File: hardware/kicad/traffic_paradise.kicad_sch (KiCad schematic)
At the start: 58 parts, among them J2 USB C, Q1 SS8050, Q2 SS8050, SW1 SW_Push, SW2 SW_Push, SW3 SW_Push, U1 ESP32-WROOM-32, U2 AMS1117-3.3, U3 USBLC6-2SC6, U4 CP2102N-A02-GQFN28

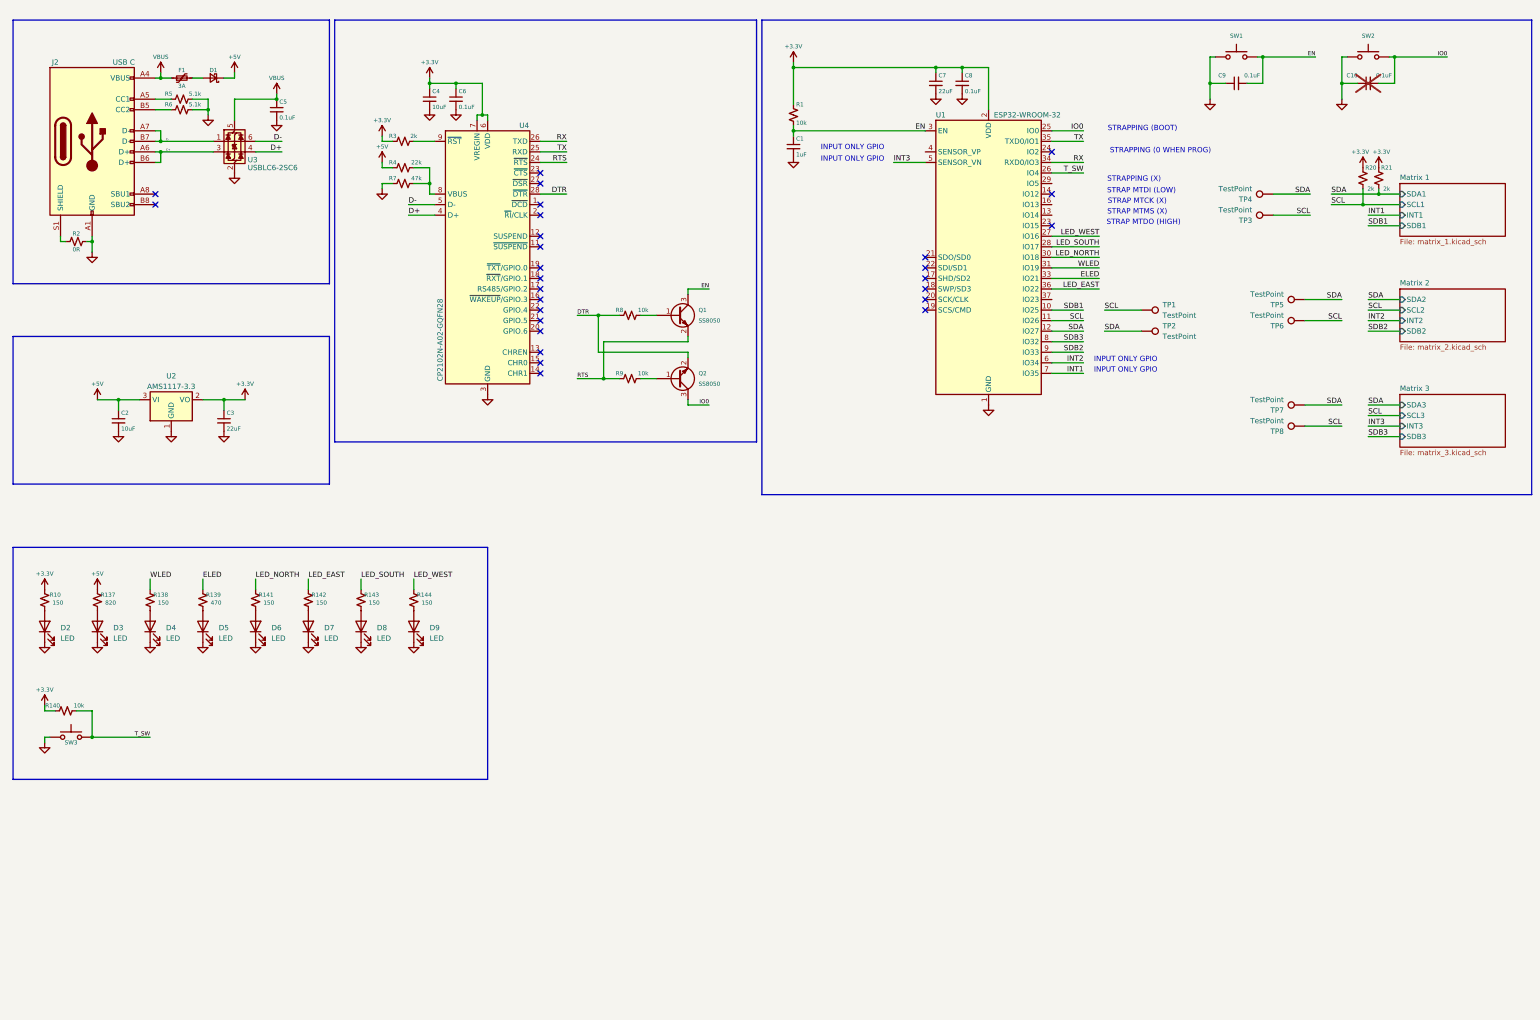
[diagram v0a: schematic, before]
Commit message: add jtag circuitry
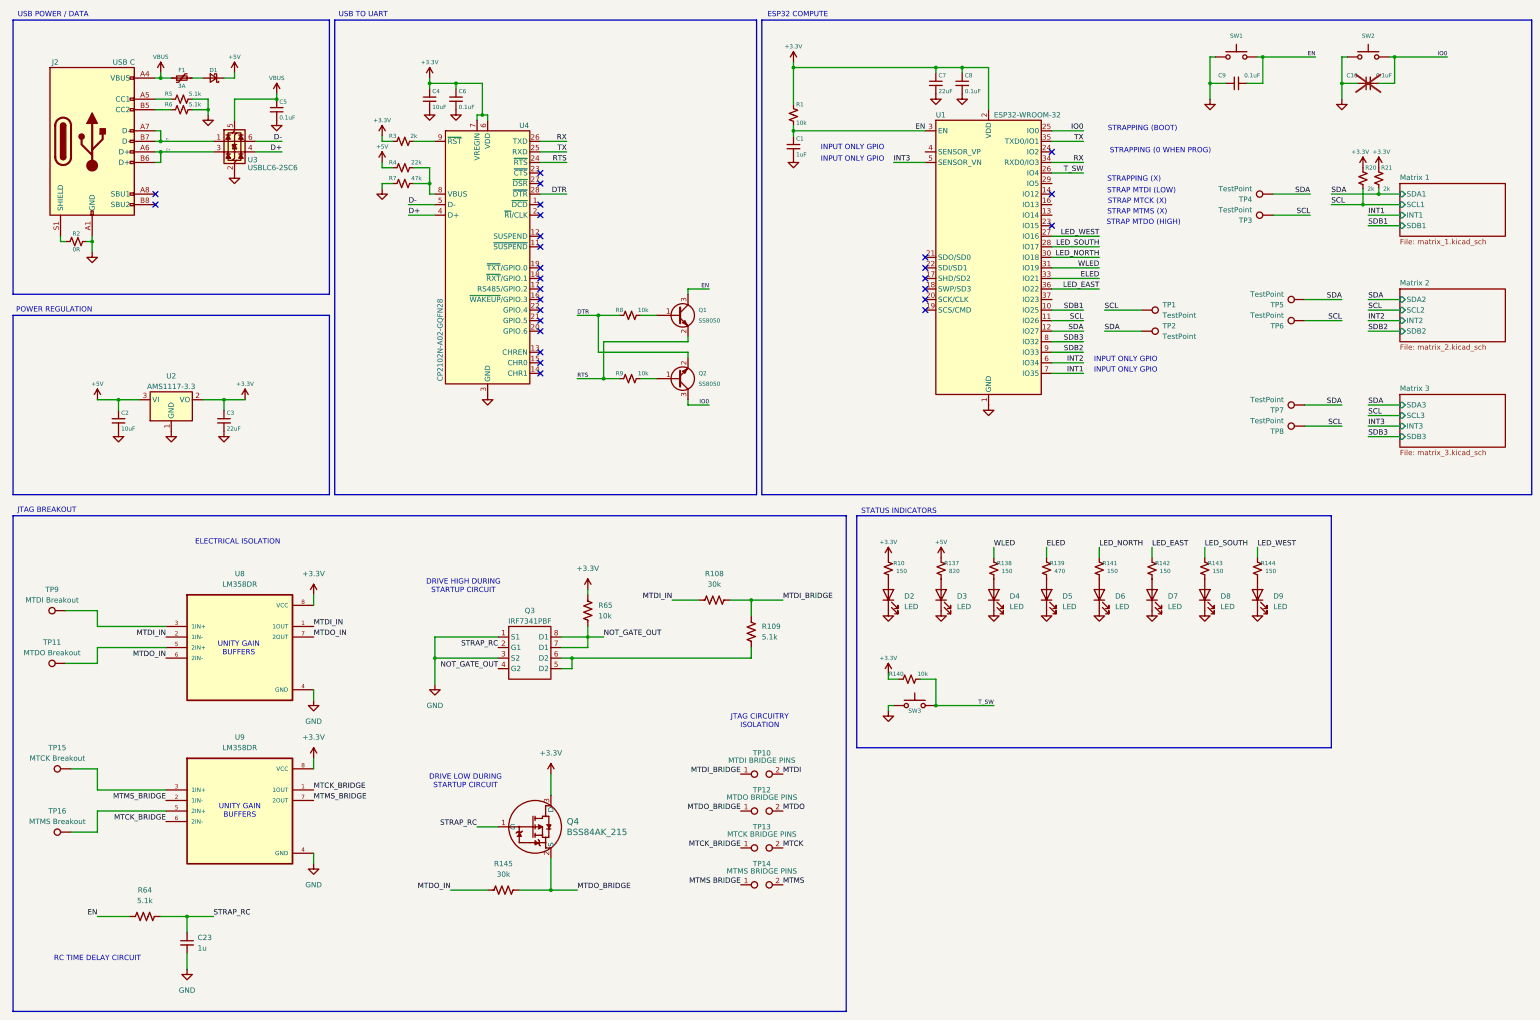
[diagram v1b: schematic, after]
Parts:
- added C23: 1u, Capacitor_SMD:C_0402_1005Metric, symbol Device:C_Small
- added Q3: IRF7341PBF, Package_SO:SOIC-8_3.9x4.9mm_P1.27mm, symbol IRF7341PBF:IRF7341PBF
- added Q4: BSS84AK_215, map_lbr:SOT23-BSS84AK_NEX, symbol BSS84AK215:BSS84AK_215
- added R108, R145: 30k, Resistor_SMD:R_0402_1005Metric, symbol Device:R_US
- added R109, R64: 5.1k, Resistor_SMD:R_0402_1005Metric, symbol Device:R_US
- added R65: 10k, Resistor_SMD:R_0603_1608Metric, symbol Device:R_US
- added TP10: MTDI BRIDGE PINS, TestPoint:TestPoint_Bridge_Pitch5.08mm_Drill1.3mm, symbol Connector:TestPoint_2Pole
- added TP11: MTDO Breakout, TestPoint:TestPoint_THTPad_D2.5mm_Drill1.2mm, symbol Connector:TestPoint
- added TP12: MTDO BRIDGE PINS, TestPoint:TestPoint_Bridge_Pitch5.08mm_Drill1.3mm, symbol Connector:TestPoint_2Pole
- added TP13: MTCK BRIDGE PINS, TestPoint:TestPoint_Bridge_Pitch5.08mm_Drill1.3mm, symbol Connector:TestPoint_2Pole
- added TP14: MTMS BRIDGE PINS, TestPoint:TestPoint_Bridge_Pitch5.08mm_Drill1.3mm, symbol Connector:TestPoint_2Pole
- added TP15: MTCK Breakout, TestPoint:TestPoint_THTPad_D2.5mm_Drill1.2mm, symbol Connector:TestPoint
- added TP16: MTMS Breakout, TestPoint:TestPoint_THTPad_D2.5mm_Drill1.2mm, symbol Connector:TestPoint
- added TP9: MTDI Breakout, TestPoint:TestPoint_THTPad_D2.5mm_Drill1.2mm, symbol Connector:TestPoint
- added U8, U9: LM358DR, map_lbr:SOIC127P599X175-8N, symbol LM358DR:LM358DR
- TP1, TP2, TP3, TP4, TP5, TP6, TP7, TP8: footprint TestPoint:TestPoint_THTPad_1.5x1.5mm_Drill0.7mm -> TestPoint:TestPoint_THTPad_D2.5mm_Drill1.2mm
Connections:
- net +3.3V: now also Q4.3 (D), R65.1, U8.8 (VCC), U9.8 (VCC)
- net EN: now also R64.1
- net GND: now also C23.2, Q3.1 (S1), Q3.3 (S2), U8.4 (GND), U9.4 (GND)
- new net: TP15.1, U9.3 (1IN+)
- new net: TP16.1, U9.5 (2IN+)
- new net: Q3.5 (D2), Q3.6 (D2), R109.1
- new net: TP9.1, U8.3 (1IN+)
- new net: TP11.1, U8.5 (2IN+)
- new net MTCK: TP13.2
- new net MTCK_BRIDGE: TP13.1, U9.1 (1OUT), U9.6 (2IN-)
- new net MTDI: TP10.2
- new net MTDI_BRIDGE: R108.2, R109.2, TP10.1
- new net MTDI_IN: R108.1, U8.1 (1OUT), U8.2 (1IN-)
- new net MTDO: TP12.2
- new net MTDO_BRIDGE: Q4.2 (S), R145.2, TP12.1
- new net MTDO_IN: R145.1, U8.6 (2IN-), U8.7 (2OUT)
- new net MTMS: TP14.2
- new net MTMS BRIDGE: TP14.1
- new net MTMS_BRIDGE: U9.2 (1IN-), U9.7 (2OUT)
- new net NOT_GATE_OUT: Q3.4 (G2), Q3.7 (D1), Q3.8 (D1), R65.2
- new net STRAP_RC: C23.1, Q3.2 (G1), Q4.1 (G), R64.2
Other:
- note added: "DRIVE HIGH DURING STARTUP CIRCUIT"
- note added: "DRIVE LOW DURING STARTUP CIRCUIT"
- note added: "ELECTRICAL ISOLATION"
- note added: "ESP32 COMPUTE"
- note added: "JTAG BREAKOUT"
- note added: "JTAG CIRCUITRY ISOLATION"
- note added: "POWER REGULATION"
- note added: "RC TIME DELAY CIRCUIT"
- note added: "STATUS INDICATORS"
- note added: "UNITY GAIN BUFFERS"
- note added: "USB POWER / DATA"
- note added: "USB TO UART"
- moved on the sheet: D2, D3, D4, D5, D6, D7, D8, D9, R10, R137, R138, R139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

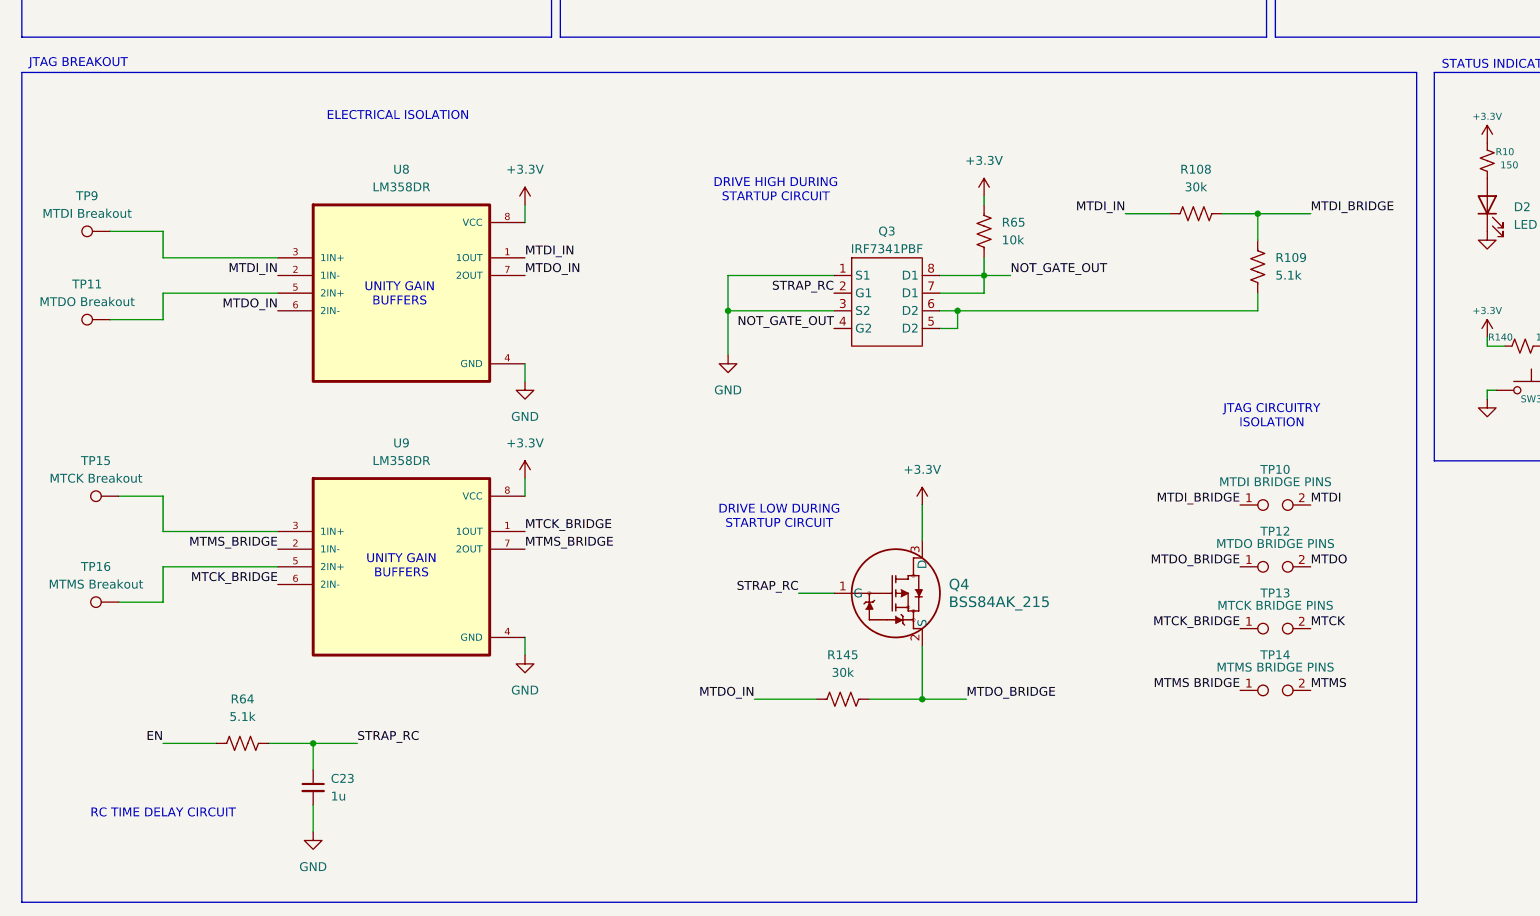
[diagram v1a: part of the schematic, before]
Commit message: change dual N-ch transistors to jlcpcb components
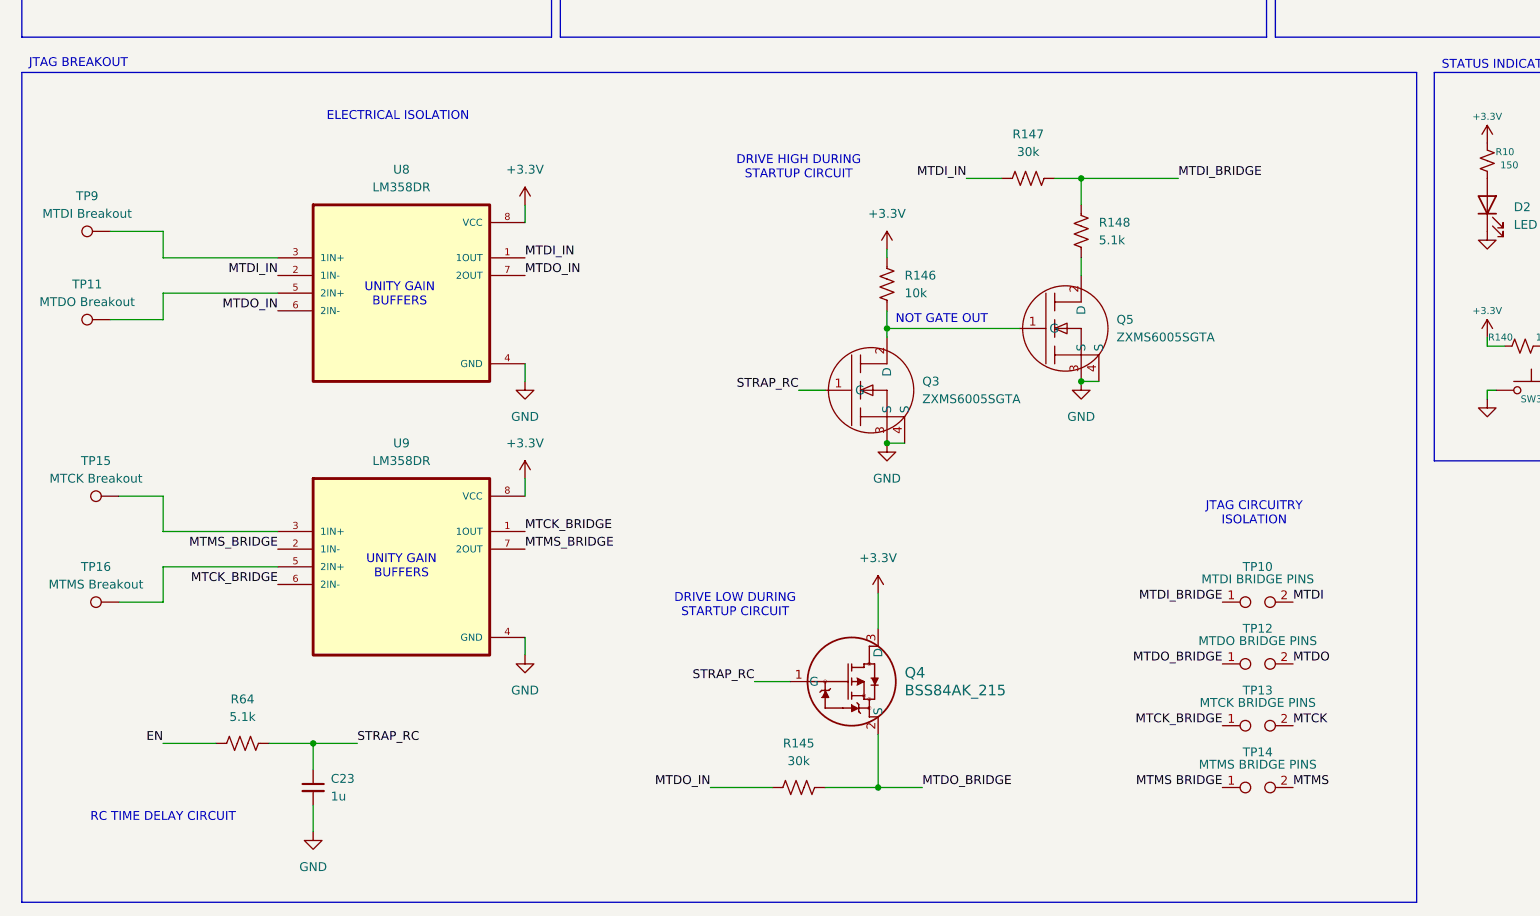
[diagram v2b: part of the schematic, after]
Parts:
- removed Q3: IRF7341PBF, Package_SO:SOIC-8_3.9x4.9mm_P1.27mm, symbol IRF7341PBF:IRF7341PBF
- removed R108: 30k, Resistor_SMD:R_0402_1005Metric, symbol Device:R_US
- removed R109: 5.1k, Resistor_SMD:R_0402_1005Metric, symbol Device:R_US
- removed R65: 10k, Resistor_SMD:R_0603_1608Metric, symbol Device:R_US
- added Q3, Q5: ZXMS6005SGTA, Package_TO_SOT_SMD:SOT-223, symbol ZXMS6005SGTA:ZXMS6005SGTA
- added R146: 10k, Resistor_SMD:R_0603_1608Metric, symbol Device:R_US
- added R147: 30k, Resistor_SMD:R_0402_1005Metric, symbol Device:R_US
- added R148: 5.1k, Resistor_SMD:R_0402_1005Metric, symbol Device:R_US
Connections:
- net +3.3V: now also R146.1
- net GND: now also Q3.3 (S), Q3.4 (S), Q5.3 (S), Q5.4 (S)
- net MTDI_BRIDGE: now also R147.2, R148.2
- net MTDI_IN: now also R147.1
- net STRAP_RC: now also Q3.1 (G)
- new net: Q5.2 (D), R148.1
- new net: Q3.2 (D), Q5.1 (G), R146.2
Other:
- note added: "NOT GATE OUT"
- moved on the sheet: Q4, R145, TP10, TP12, TP13, TP14

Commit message: route jtag components & few fixes
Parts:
- renumbered TP15 to MTCK1, TP13 to MTCK_BR1, TP9 to MTDI1, TP10 to MTDI_BR1, TP11 to MTDO1, TP12 to MTDO_BR1, TP16 to MTMS1, TP14 to MTMS_BR1, TP1 to SCL1, TP3 to SCL2, TP6 to SCL3, TP8 to SCL4, TP2 to SDA1, TP4 to SDA2, TP5 to SDA3, TP7 to SDA4
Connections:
- net MTMS BRIDGE is gone; now on net MTMS_BRIDGE: MTMS_BR1.1
- net MTCK: now also U1.16 (IO13)
- net MTCK_BRIDGE: now also U9.2 (1IN-); no longer U9.6 (2IN-)
- net MTDI: now also U1.14 (IO12)
- net MTDO: now also U1.23 (IO15)
- net MTMS: now also U1.13 (IO14)
- net MTMS_BRIDGE: now also U9.6 (2IN-); no longer U9.2 (1IN-)
- no-connect marks 27 -> 26
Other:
- moved on the sheet: SCL2, SCL3, SCL4
